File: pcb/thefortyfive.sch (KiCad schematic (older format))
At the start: 106 parts, among them J1 Conn_01x16_Female, J2 Conn_01x12_Female

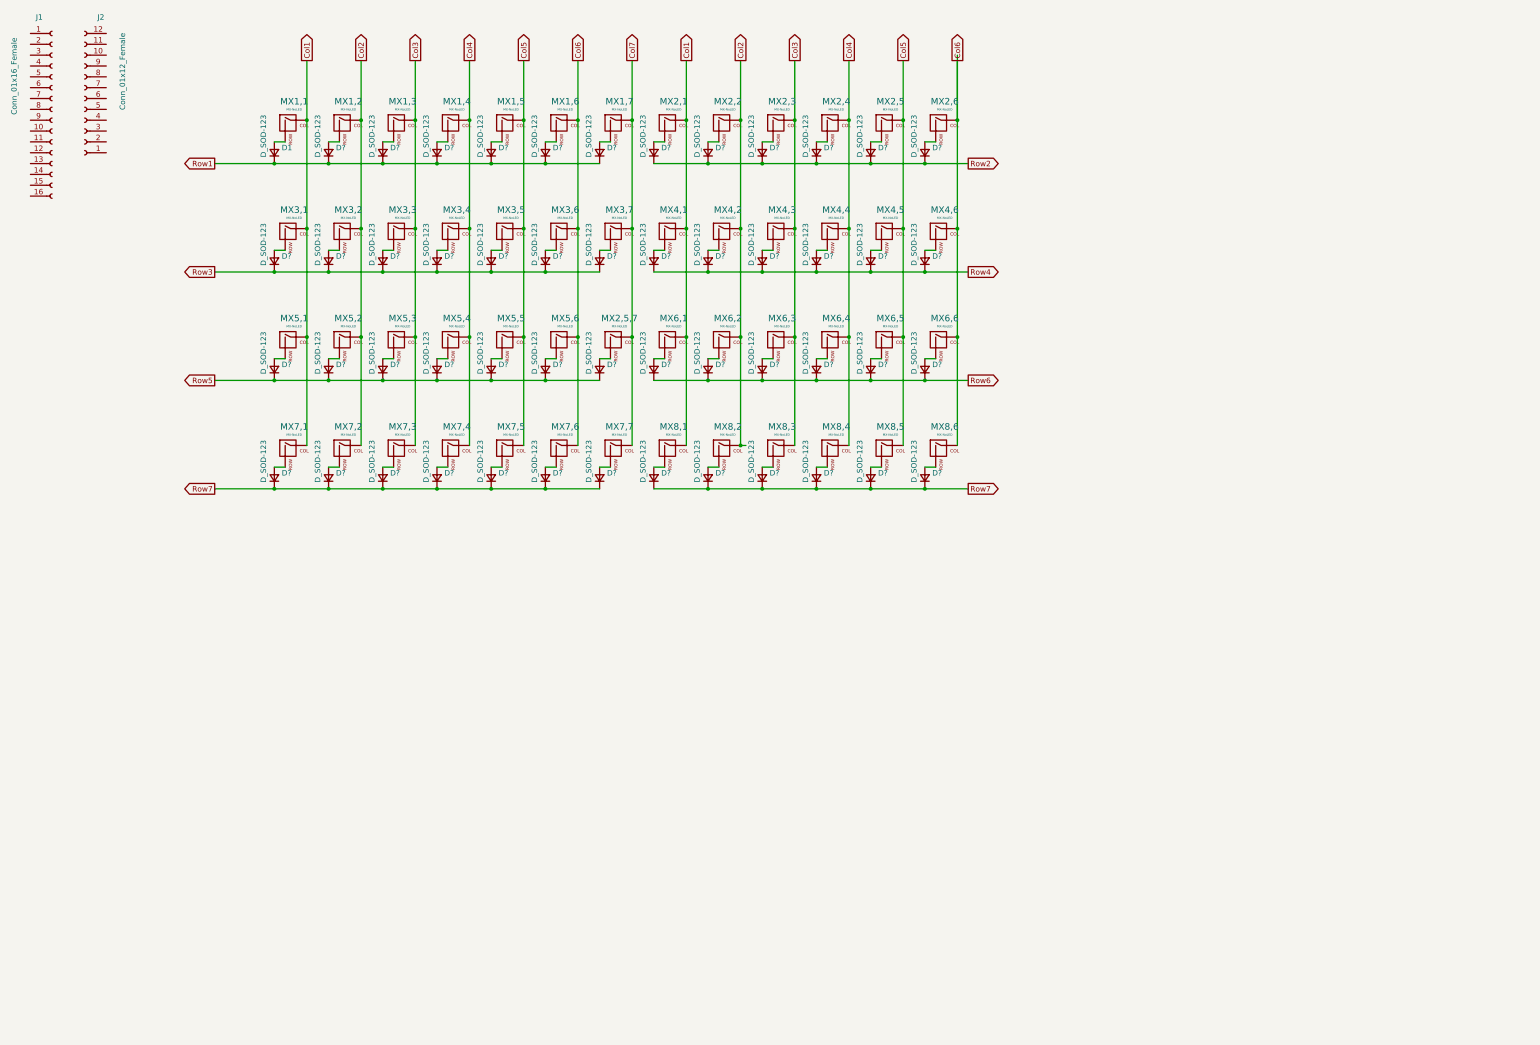
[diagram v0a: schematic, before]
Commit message: add optional switches
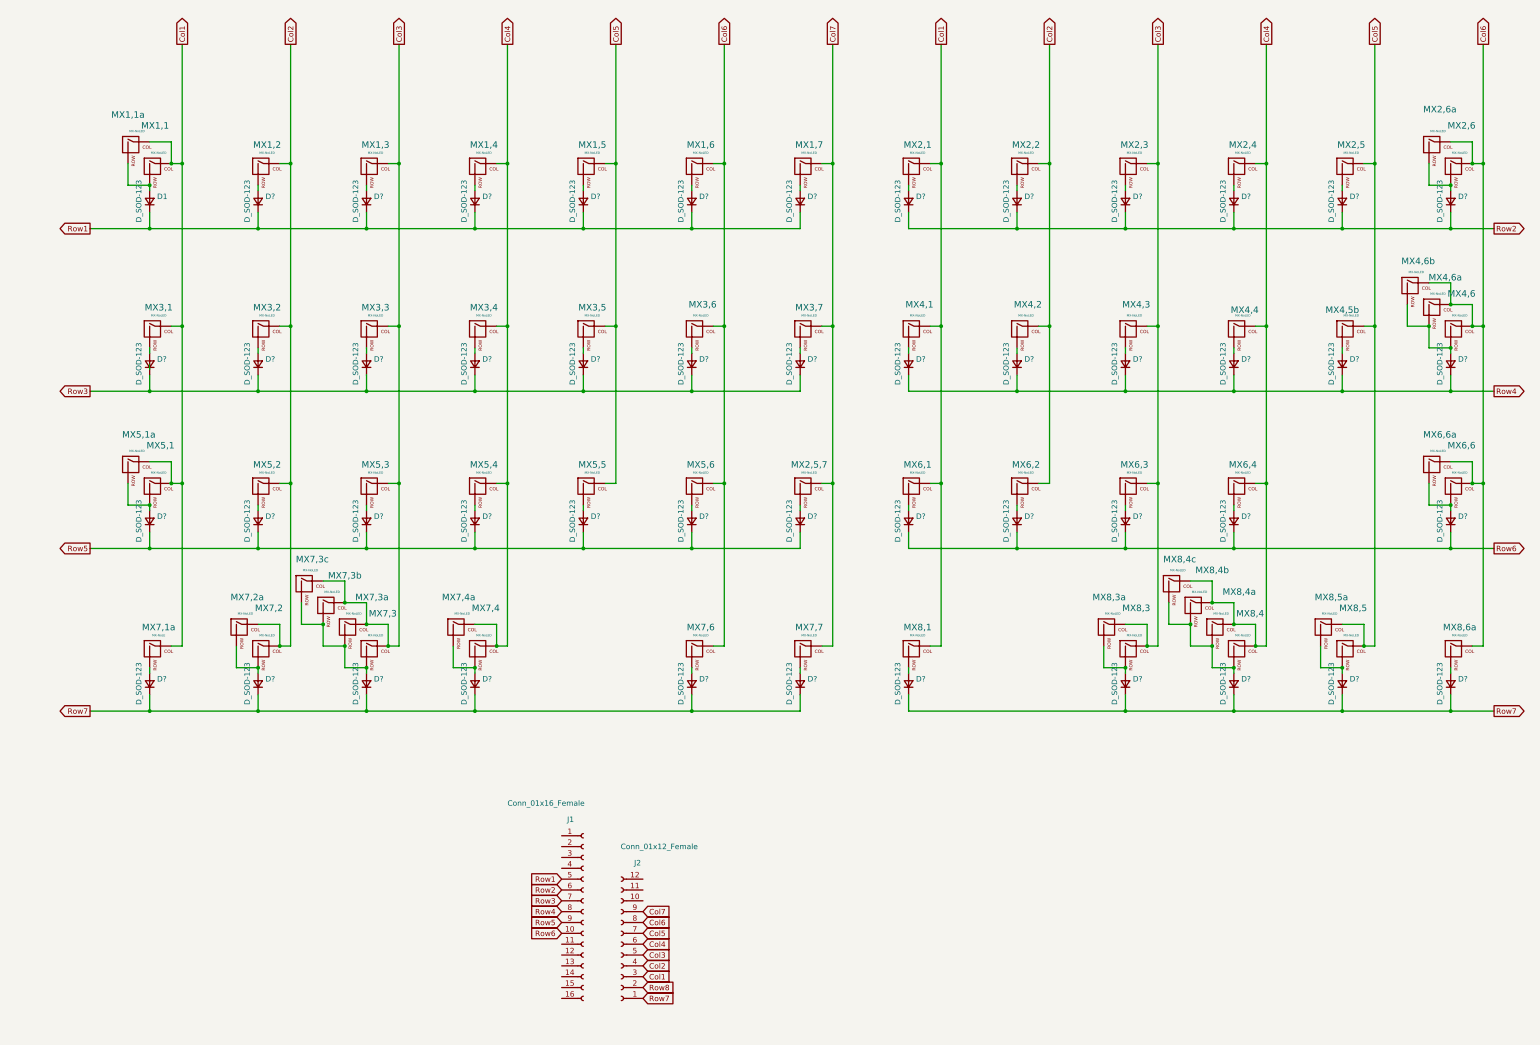
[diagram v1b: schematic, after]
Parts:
- removed D? (x3): D_SOD-123, Diode_SMD:D_SOD-123, symbol Device:D_Small
- removed MX6,5, MX7,5, MX8,2: MX-NoLED, MX_Alps_Hybrid:MXOnly-1U, symbol MX_Alps_Hybrid:MX-NoLED
- added MX1,1a, MX2,6a, MX4,6a, MX4,6b, MX5,1a, MX6,6a, MX7,2a, MX7,3a, MX7,3b, MX7,3c, MX7,4a, MX8,3a, MX8,4a, MX8,4b, MX8,4c, MX8,5a: MX-NoLED, MX_Alps_Hybrid:MXOnly-1U, symbol MX_Alps_Hybrid:MX-NoLED
- MX7,1a: renamed from MX7,1; value MX-NoLED -> MX-NoLE
- renumbered MX4,5 to MX4,5b, MX8,6 to MX8,6a
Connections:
- net Col1: now also J2.3 (Pin_3), MX1,1a.1 (COL), MX5,1a.1 (COL)
- net Col2: now also J2.4 (Pin_4), MX7,2a.1 (COL)
- net Col3: now also J2.5 (Pin_5), MX7,3a.1 (COL), MX7,3b.1 (COL), MX7,3c.1 (COL), MX8,3a.1 (COL)
- net Col4: now also J2.6 (Pin_6), MX7,4a.1 (COL), MX8,4a.1 (COL), MX8,4b.1 (COL), MX8,4c.1 (COL)
- net Col5: now also J2.7 (Pin_7), MX8,5a.1 (COL)
- net Col6: now also J2.8 (Pin_8), MX2,6a.1 (COL), MX4,6a.1 (COL), MX4,6b.1 (COL), MX6,6a.1 (COL)
- net Col7: now also J2.9 (Pin_9)
- net Row1: now also J1.5 (Pin_5)
- net Row2: now also J1.6 (Pin_6)
- net Row3: now also J1.7 (Pin_7)
- net Row4: now also J1.8 (Pin_8)
- net Row5: now also J1.9 (Pin_9)
- net Row6: now also J1.10 (Pin_10)
- net Row7: now also J2.1 (Pin_1)
- net Row8: now reaches J2.2 (Pin_2)
- net at D1.2 (A), MX1,1.2 (ROW): now also MX1,1a.2 (ROW)
- net at D?.2 (A), MX2,6.2 (ROW): now also MX2,6a.2 (ROW)
- net at D?.2 (A), MX4,6.2 (ROW): now also MX4,6a.2 (ROW), MX4,6b.2 (ROW)
- net at D?.2 (A), MX5,1.2 (ROW): now also MX5,1a.2 (ROW)
- net at D?.2 (A), MX6,6.2 (ROW): now also MX6,6a.2 (ROW)
- net at D?.2 (A), MX7,2.2 (ROW): now also MX7,2a.2 (ROW)
- net at D?.2 (A), MX7,3.2 (ROW): now also MX7,3a.2 (ROW), MX7,3b.2 (ROW), MX7,3c.2 (ROW)
- net at D?.2 (A), MX7,4.2 (ROW): now also MX7,4a.2 (ROW)
- net at D?.2 (A), MX8,3.2 (ROW): now also MX8,3a.2 (ROW)
- net at D?.2 (A), MX8,4.2 (ROW): now also MX8,4a.2 (ROW), MX8,4b.2 (ROW), MX8,4c.2 (ROW)
- net at D?.2 (A), MX8,5.2 (ROW): now also MX8,5a.2 (ROW)
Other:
- moved on the sheet: D1, D?, J1, J2, MX1,1, MX1,2, MX1,3, MX1,4, MX1,5, MX1,6, MX1,7, MX2,1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

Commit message: add sizing for switch footprints
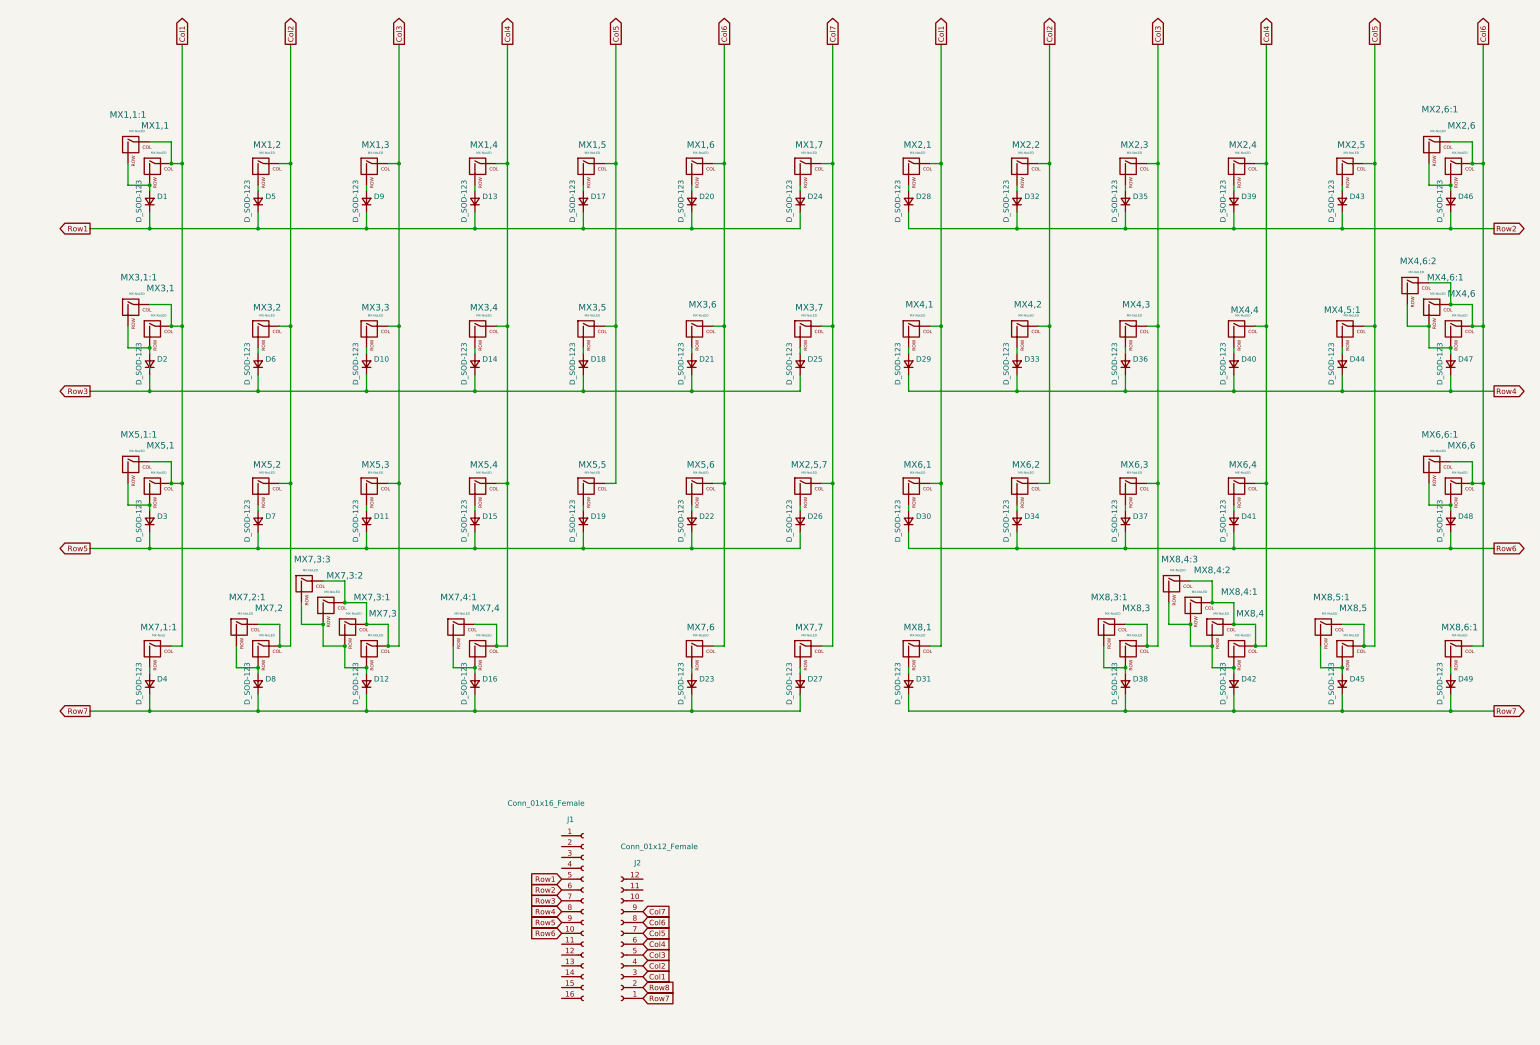
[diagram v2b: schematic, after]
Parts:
- added MX3,1:1: MX-NoLED, MX_Alps_Hybrid:MXOnly-1.75U, symbol MX_Alps_Hybrid:MX-NoLED
- MX1,1:1: renamed from MX1,1a; footprint MX_Alps_Hybrid:MXOnly-1U -> MX_Alps_Hybrid:MXOnly-1.5U
- MX2,6:1: renamed from MX2,6a; footprint MX_Alps_Hybrid:MXOnly-1U -> MX_Alps_Hybrid:MXOnly-1.5U
- MX3,1, MX6,6, MX7,3, MX8,4: footprint MX_Alps_Hybrid:MXOnly-1U -> MX_Alps_Hybrid:MXOnly-1.25U
- MX4,6, MX5,1: footprint MX_Alps_Hybrid:MXOnly-1U -> MX_Alps_Hybrid:MXOnly-1.75U
- MX4,6:1: renamed from MX4,6a; footprint MX_Alps_Hybrid:MXOnly-1U -> MX_Alps_Hybrid:MXOnly-2,25U
- MX4,6:2: renamed from MX4,6b; footprint MX_Alps_Hybrid:MXOnly-1U -> MX_Alps_Hybrid:MXOnly-1.25U
- MX5,1:1: renamed from MX5,1a; footprint MX_Alps_Hybrid:MXOnly-1U -> MX_Alps_Hybrid:MXOnly-2,25U
- MX6,6:1: renamed from MX6,6a; footprint MX_Alps_Hybrid:MXOnly-1U -> MX_Alps_Hybrid:MXOnly-1.75U
- MX7,1:1: renamed from MX7,1a; footprint MX_Alps_Hybrid:MXOnly-1U -> MX_Alps_Hybrid:MXOnly-1.25U
- MX7,3:3: renamed from MX7,3c; footprint MX_Alps_Hybrid:MXOnly-1U -> MX_Alps_Hybrid:MXOnly-1.25U
- MX7,4:1: renamed from MX7,4a; footprint MX_Alps_Hybrid:MXOnly-1U -> MX_Alps_Hybrid:MXOnly-1.25U
- MX7,6: footprint MX_Alps_Hybrid:MXOnly-1U -> MX_Alps_Hybrid:MXOnly-2.25U
- MX7,7: footprint MX_Alps_Hybrid:MXOnly-1U -> MX_Alps_Hybrid:MXOnly-7U
- MX8,1: footprint MX_Alps_Hybrid:MXOnly-1U -> MX_Alps_Hybrid:MXOnly-2.75U
- MX8,3:1: renamed from MX8,3a; footprint MX_Alps_Hybrid:MXOnly-1U -> MX_Alps_Hybrid:MXOnly-1.25U
- MX8,4:3: renamed from MX8,4c; footprint MX_Alps_Hybrid:MXOnly-1U -> MX_Alps_Hybrid:MXOnly-1.25U
- MX8,6:1: renamed from MX8,6a; footprint MX_Alps_Hybrid:MXOnly-1U -> MX_Alps_Hybrid:MXOnly-1.25U
- gave numbers to parts that had none: 48
- renumbered MX4,5b to MX4,5:1, MX7,2a to MX7,2:1, MX7,3a to MX7,3:1, MX7,3b to MX7,3:2, MX8,4a to MX8,4:1, MX8,4b to MX8,4:2, MX8,5a to MX8,5:1
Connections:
- net Col1: now also MX3,1:1.1 (COL)
- net at D2.2 (A), MX3,1.2 (ROW): now also MX3,1:1.2 (ROW)

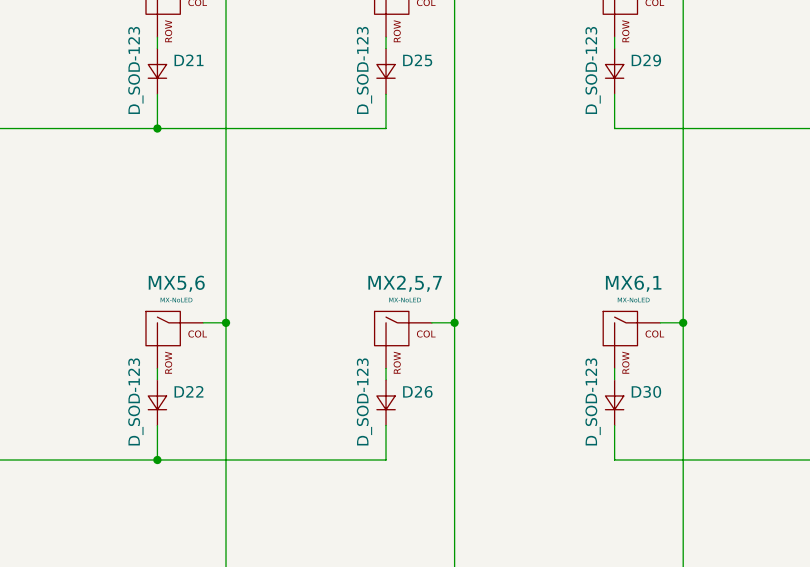
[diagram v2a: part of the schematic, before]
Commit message: add edge cut
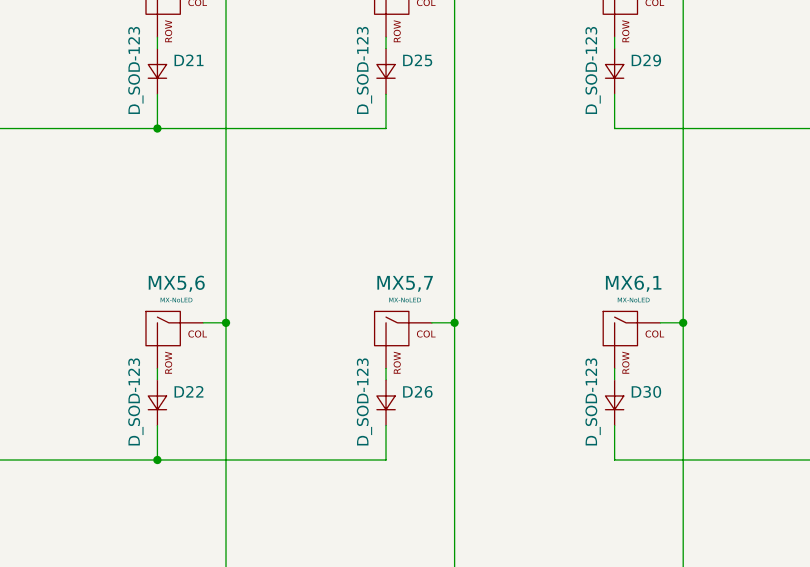
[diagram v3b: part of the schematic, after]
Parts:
- renumbered MX2,5,7 to MX5,7
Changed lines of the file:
@@
 $EndComp
 $Comp
-L MX_Alps_Hybrid:MX-NoLED MX2,5,7
+L MX_Alps_Hybrid:MX-NoLED MX5,7
 U 1 1 5E929897
 P 7850 4950
-F 0 "MX2,5,7" H 7883 5173 60  0000 C CNN
+F 0 "MX5,7" H 7883 5173 60  0000 C CNN
 F 1 "MX-NoLED" H 7883 5099 20  0000 C CNN
 F 2 "MX_Alps_Hybrid:MXOnly-1U" H 7225 4925 60  0001 C CNN

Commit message: add routing
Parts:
- MX4,6:1, MX5,1:1: footprint MX_Alps_Hybrid:MXOnly-2,25U -> MX_Alps_Hybrid:MXOnly-2.25U
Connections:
- net Col1: now also J2.2 (Pin_2); no longer J2.3 (Pin_3)
- net Col2: now also J2.3 (Pin_3); no longer J2.4 (Pin_4)
- net Col3: now also J2.4 (Pin_4); no longer J2.5 (Pin_5)
- net Col4: now also J2.5 (Pin_5); no longer J2.6 (Pin_6)
- net Col5: now also J2.6 (Pin_6); no longer J2.7 (Pin_7)
- net Col6: now also J2.7 (Pin_7); no longer J2.8 (Pin_8)
- net Col7: now also J2.8 (Pin_8); no longer J2.9 (Pin_9)
- net Row1: now also J1.10 (Pin_10); no longer J1.5 (Pin_5)
- net Row2: now also J1.5 (Pin_5); no longer J1.6 (Pin_6)
- net Row3: now also J1.9 (Pin_9); no longer J1.7 (Pin_7)
- net Row4: now also J1.6 (Pin_6); no longer J1.8 (Pin_8)
- net Row5: now also J1.8 (Pin_8); no longer J1.9 (Pin_9)
- net Row6: now also J1.7 (Pin_7); no longer J1.10 (Pin_10)
- net Row7: now also J2.9 (Pin_9); no longer D31.1 (K), D38.1 (K), D42.1 (K), D45.1 (K), D49.1 (K), J2.1 (Pin_1)
- net Row8: now also D31.1 (K), D38.1 (K), D42.1 (K), D45.1 (K), D49.1 (K), J2.1 (Pin_1); no longer J2.2 (Pin_2)
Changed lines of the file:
@@
 Row6
 Text GLabel 14200 7000 2    50   Output ~ 0
-Row7
+Row8
 Text GLabel 11100 850  1    50   Output ~ 0
 Col3
@@
 F 0 "MX4,6:1" H 13750 3600 60  0000 C CNN
 F 1 "MX-NoLED" H 13683 3449 20  0000 C CNN
-F 2 "MX_Alps_Hybrid:MXOnly-2,25U" H 13025 3275 60  0001 C CNN
+F 2 "MX_Alps_Hybrid:MXOnly-2.25U" H 13025 3275 60  0001 C CNN
 F 3 "" H 13025 3275 60  0001 C CNN
 	1    13650 3300
@@
 F 0 "MX5,1:1" H 1700 5050 60  0000 C CNN
 F 1 "MX-NoLED" H 1683 4899 20  0000 C CNN
-F 2 "MX_Alps_Hybrid:MXOnly-2,25U" H 1025 4725 60  0001 C CNN
+F 2 "MX_Alps_Hybrid:MXOnly-2.25U" H 1025 4725 60  0001 C CNN
 F 3 "" H 1025 4725 60  0001 C CNN
 	1    1650 4750
@@
 Wire Wire Line
 	13800 7000 14200 7000
+Text GLabel 5600 9050 0    50   Input ~ 0
+Row1
 Text GLabel 5600 8550 0    50   Input ~ 0
-Row1
+Row2
+Text GLabel 5600 8950 0    50   Input ~ 0
+Row3
 Text GLabel 5600 8650 0    50   Input ~ 0
-Row2
+Row4
+Text GLabel 5600 8850 0    50   Input ~ 0
+Row5
 Text GLabel 5600 8750 0    50   Input ~ 0
-Row3
-Text GLabel 5600 8850 0    50   Input ~ 0
-Row4
-Text GLabel 5600 8950 0    50   Input ~ 0
-Row5
-Text GLabel 5600 9050 0    50   Input ~ 0
 Row6
+Text GLabel 6350 8850 2    50   Input ~ 0
+Row7
 Text GLabel 6350 9650 2    50   Input ~ 0
-Row7
+Row8
 Text GLabel 6350 9550 2    50   Input ~ 0
-Row8
+Col1
 Text GLabel 6350 9450 2    50   Input ~ 0
-Col1
+Col2
 Text GLabel 6350 9350 2    50   Input ~ 0
-Col2
+Col3
 Text GLabel 6350 9250 2    50   Input ~ 0
-Col3
+Col4
 Text GLabel 6350 9150 2    50   Input ~ 0
-Col4
+Col5
 Text GLabel 6350 9050 2    50   Input ~ 0
-Col5
+Col6
 Text GLabel 6350 8950 2    50   Input ~ 0
-Col6
-Text GLabel 6350 8850 2    50   Input ~ 0
 Col7
 $Comp

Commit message: add ground fills
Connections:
- net GND: now reaches J1.4 (Pin_4)
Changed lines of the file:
@@
 	1600 3650 1800 3650
 Connection ~ 1800 3650
+Text GLabel 5600 8450 0    50   Input ~ 0
+GND
 $EndSCHEMATC

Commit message: add switch labels
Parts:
- MX1,1, MX1,2, MX1,3, MX1,4, MX1,5, MX1,6, MX1,7, MX2,1, MX2,2, MX2,3, MX2,4, MX2,5, MX2,6, MX3,2, MX3,3, MX3,4, MX3,5, MX3,6, MX3,7, MX4,1, MX4,2, MX4,3, MX4,4, MX4,5:1, MX5,2, MX5,3, MX5,4, MX5,5, MX5,6, MX5,7, MX6,1, MX6,2, MX6,3, MX6,4, MX7,2, MX7,2:1, MX7,3:1, MX7,3:2, MX7,4, MX8,3, MX8,4:1, MX8,4:2, MX8,5, MX8,5:1: footprint MX_Alps_Hybrid:MXOnly-1U -> MX_Alps_Hybrid:MXOnly-1U-NoLED
- MX1,1:1, MX2,6:1: footprint MX_Alps_Hybrid:MXOnly-1.5U -> MX_Alps_Hybrid:MXOnly-1.5U-NoLED
- MX3,1, MX4,6:2, MX6,6, MX7,1:1, MX7,3, MX7,3:3, MX7,4:1, MX8,3:1, MX8,4, MX8,4:3, MX8,6:1: footprint MX_Alps_Hybrid:MXOnly-1.25U -> MX_Alps_Hybrid:MXOnly-1.25U-NoLED
- MX3,1:1, MX4,6, MX5,1, MX6,6:1: footprint MX_Alps_Hybrid:MXOnly-1.75U -> MX_Alps_Hybrid:MXOnly-1.75U-NoLED
- MX4,6:1, MX5,1:1, MX7,6: footprint MX_Alps_Hybrid:MXOnly-2.25U -> MX_Alps_Hybrid:MXOnly-2.25U-NoLED
- MX7,7: footprint MX_Alps_Hybrid:MXOnly-7U -> MX_Alps_Hybrid:MXOnly-7U-NoLED
- MX8,1: footprint MX_Alps_Hybrid:MXOnly-2.75U -> MX_Alps_Hybrid:MXOnly-2.75U-NoLED
